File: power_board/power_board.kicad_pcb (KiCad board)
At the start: 2 copper layers, 171.8 x 117.7 mm, 86 parts, among them J1 PROG, J10 M4, J11 5V_1, J12 M5, J13 M6, J14 M7, J15 FAN, J16 Screw_Terminal_01x02, J17 MB_interface, J18 Conn_01x02_Female, J19 12V_1, J2 M1, J20 12V_2, J21 12V_3, J22 12V_4, J23 48V_1, J24 48V_2, J25 48V_3, J26 48V_4, J27 Screw_Terminal_01x02, J3 M2, J4 Conn_01x02_Female, J5 Conn_01x02_Female, J6 Conn_01x01_Male, J7 Conn_01x01_Male, J8 Screw_Terminal_01x02, J9 M3, Q1 Q_NPN_BEC, SW1 SW_Push, U1 ACS758xCB-050B-PFF, U10 MAX31855KASA, U2 ACS758xCB-050B-PFF, U3 MCP2515-EST, U4 MAX31855KASA, U5 ATA6560,1, U6 BTS50085-1TMA, U7 ATmega328P-AU, U8 BTS50085-1TMA, U9 LM2596S-5, Y1 20Mhz, Y2 16Mhz

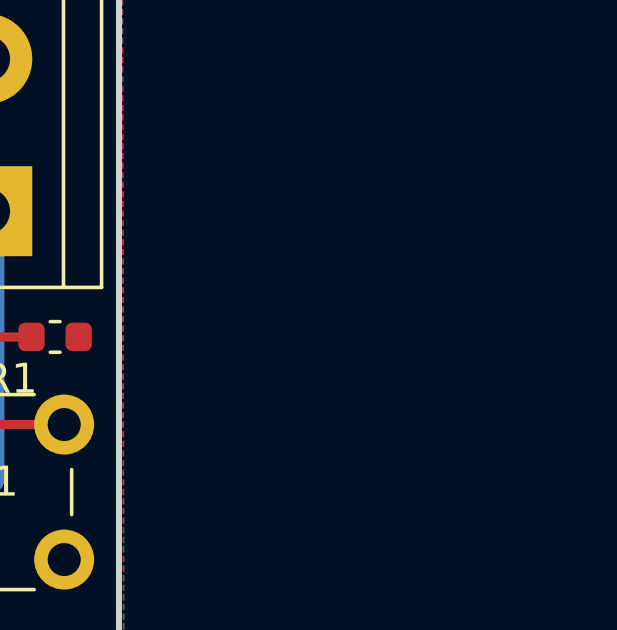
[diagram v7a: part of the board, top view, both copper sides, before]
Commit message: Adding 3.3v regulator hardware for TC amps
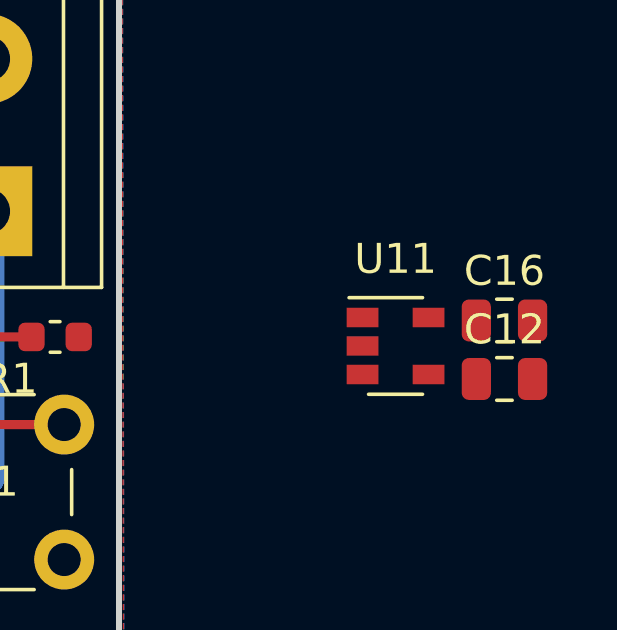
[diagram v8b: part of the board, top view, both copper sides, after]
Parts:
- added C12: 10uF, Capacitor_SMD:C_0805_2012Metric, F.Cu at (238.9, 72.1)
- added C16: 10uF, Capacitor_SMD:C_0805_2012Metric, F.Cu at (238.9, 70.2)
- added U11: TLV75533PDBV, Package_TO_SOT_SMD:SOT-23-5, F.Cu at (235.2, 71.0)
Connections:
- C10 pad 1: +5V -> V_MCU
- C5 pad 1: +5V -> V_MCU
- C6 pad 1: +5V -> +3V3
- C7 pad 1: +5V -> +3V3
- R10 pad 1: +5V -> +3V3
- R8 pad 1: +5V -> +3V3
- U10 pad 4: +5V -> +3V3
- U3 pad 20: +5V -> V_MCU
- U4 pad 4: +5V -> +3V3
- U5 pad 3: +5V -> V_MCU
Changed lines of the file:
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@@
     (tracks 867)
     (zones 0)
-    (modules 86)
-    (nets 68)
+    (modules 89)
+    (nets 70)
   )
   (page A4)
@@
   (net 66 V_MCU)
   (net 67 "Net-(R9-Pad1)")
+  (net 68 +3V3)
+  (net 69 "Net-(U11-Pad4)")
   (net_class Default "This is the default net class."
     (clearance 0.2)
@@
     (add_net +12V)
     (add_net +12VA)
+    (add_net +3V3)
     (add_net +48V)
     (add_net +5V)
@@
     (add_net "Net-(REG1-Pad5)")
     (add_net "Net-(REG2-Pad5)")
+    (add_net "Net-(U11-Pad4)")
     (add_net "Net-(U3-Pad3)")
     (add_net "Net-(U3-Pad6)")
@@
     (add_net V_MCU)
   )
+  (module Capacitor_SMD:C_0805_2012Metric (layer F.Cu)
+    (at 238.854001 72.140001)
+    (descr "Capacitor SMD 0805 (2012 Metric), square (rectangular) end terminal, IPC_7351 nominal, (Body size source: https://docs.google.com/spreadsheets/d/1BsfQQcO9C6DZCsRaXUlFlo91Tg2WpOkGARC1WS5S8t0/edit?usp=sharing), generated with kicad-footprint-generator")
+    (tags capacitor)
+    (attr smd)
+    (fp_text reference C12 (at 0 -1.65) (layer F.SilkS)
+      (effects (font (size 1 1) (thickness 0.15)))
+    )
+    (fp_text value 10uF (at 0 1.65) (layer F.Fab)
+      (effects (font (size 1 1) (thickness 0.15)))
+    )
+    (fp_text user %R (at 0 0) (layer F.Fab)
+      (effects (font (size 0.5 0.5) (thickness 0.08)))
+    )
+    (fp_line (start 1.68 0.95) (end -1.68 0.95) (layer F.CrtYd) (width 0.05))
+    (fp_line (start 1.68 -0.95) (end 1.68 0.95) (layer F.CrtYd) (width 0.05))
+    (fp_line (start -1.68 -0.95) (end 1.68 -0.95) (layer F.CrtYd) (width 0.05))
+    (fp_line (start -1.68 0.95) (end -1.68 -0.95) (layer F.CrtYd) (width 0.05))
+    (fp_line (start -0.258578 0.71) (end 0.258578 0.71) (layer F.SilkS) (width 0.12))
+    (fp_line (start -0.258578 -0.71) (end 0.258578 -0.71) (layer F.SilkS) (width 0.12))
+    (fp_line (start 1 0.6) (end -1 0.6) (layer F.Fab) (width 0.1))
+    (fp_line (start 1 -0.6) (end 1 0.6) (layer F.Fab) (width 0.1))
+    (fp_line (start -1 -0.6) (end 1 -0.6) (layer F.Fab) (width 0.1))
+    (fp_line (start -1 0.6) (end -1 -0.6) (layer F.Fab) (width 0.1))
+    (pad 2 smd roundrect (at 0.9375 0) (size 0.975 1.4) (layers F.Cu F.Paste F.Mask) (roundrect_rratio 0.25)
+      (net 5 GNDREF))
+    (pad 1 smd roundrect (at -0.9375 0) (size 0.975 1.4) (layers F.Cu F.Paste F.Mask) (roundrect_rratio 0.25)
+      (net 66 V_MCU))
+    (model ${KISYS3DMOD}/Capacitor_SMD.3dshapes/C_0805_2012Metric.wrl
+      (at (xyz 0 0 0))
+      (scale (xyz 1 1 1))
+      (rotate (xyz 0 0 0))
+    )
+  )
+  (module Capacitor_SMD:C_0805_2012Metric (layer F.Cu)
+    (at 238.854001 70.190001)
+    (descr "Capacitor SMD 0805 (2012 Metric), square (rectangular) end terminal, IPC_7351 nominal, (Body size source: https://docs.google.com/spreadsheets/d/1BsfQQcO9C6DZCsRaXUlFlo91Tg2WpOkGARC1WS5S8t0/edit?usp=sharing), generated with kicad-footprint-generator")
+    (tags capacitor)
+    (attr smd)
+    (fp_text reference C16 (at 0 -1.65) (layer F.SilkS)
+      (effects (font (size 1 1) (thickness 0.15)))
+    )
+    (fp_text value 10uF (at 0 1.65) (layer F.Fab)
+      (effects (font (size 1 1) (thickness 0.15)))
+    )
+    (fp_line (start -1 0.6) (end -1 -0.6) (layer F.Fab) (width 0.1))
+    (fp_line (start -1 -0.6) (end 1 -0.6) (layer F.Fab) (width 0.1))
+    (fp_line (start 1 -0.6) (end 1 0.6) (layer F.Fab) (width 0.1))
+    (fp_line (start 1 0.6) (end -1 0.6) (layer F.Fab) (width 0.1))
+    (fp_line (start -0.258578 -0.71) (end 0.258578 -0.71) (layer F.SilkS) (width 0.12))
+    (fp_line (start -0.258578 0.71) (end 0.258578 0.71) (layer F.SilkS) (width 0.12))
+    (fp_line (start -1.68 0.95) (end -1.68 -0.95) (layer F.CrtYd) (width 0.05))
+    (fp_line (start -1.68 -0.95) (end 1.68 -0.95) (layer F.CrtYd) (width 0.05))
+    (fp_line (start 1.68 -0.95) (end 1.68 0.95) (layer F.CrtYd) (width 0.05))
+    (fp_line (start 1.68 0.95) (end -1.68 0.95) (layer F.CrtYd) (width 0.05))
+    (fp_text user %R (at 0 0) (layer F.Fab)
+      (effects (font (size 0.5 0.5) (thickness 0.08)))
+    )
+    (pad 1 smd roundrect (at -0.9375 0) (size 0.975 1.4) (layers F.Cu F.Paste F.Mask) (roundrect_rratio 0.25)
+      (net 68 +3V3))
+    (pad 2 smd roundrect (at 0.9375 0) (size 0.975 1.4) (layers F.Cu F.Paste F.Mask) (roundrect_rratio 0.25)
+      (net 5 GNDREF))
+    (model ${KISYS3DMOD}/Capacitor_SMD.3dshapes/C_0805_2012Metric.wrl
+      (at (xyz 0 0 0))
+      (scale (xyz 1 1 1))
+      (rotate (xyz 0 0 0))
+    )
+  )
+  (module Package_TO_SOT_SMD:SOT-23-5 (layer F.Cu)
+    (at 235.224001 71.040001)
+    (descr "5-pin SOT23 package")
+    (tags SOT-23-5)
+    (attr smd)
+    (fp_text reference U11 (at 0 -2.9) (layer F.SilkS)
+      (effects (font (size 1 1) (thickness 0.15)))
+    )
+    (fp_text value TLV75533PDBV (at 0 2.9) (layer F.Fab)
+      (effects (font (size 1 1) (thickness 0.15)))
+    )
+    (fp_text user %R (at 0 0 90) (layer F.Fab)
+      (effects (font (size 0.5 0.5) (thickness 0.075)))
+    )
+    (fp_line (start -0.9 1.61) (end 0.9 1.61) (layer F.SilkS) (width 0.12))
+    (fp_line (start 0.9 -1.61) (end -1.55 -1.61) (layer F.SilkS) (width 0.12))
+    (fp_line (start -1.9 -1.8) (end 1.9 -1.8) (layer F.CrtYd) (width 0.05))
+    (fp_line (start 1.9 -1.8) (end 1.9 1.8) (layer F.CrtYd) (width 0.05))
+    (fp_line (start 1.9 1.8) (end -1.9 1.8) (layer F.CrtYd) (width 0.05))
+    (fp_line (start -1.9 1.8) (end -1.9 -1.8) (layer F.CrtYd) (width 0.05))
+    (fp_line (start -0.9 -0.9) (end -0.25 -1.55) (layer F.Fab) (width 0.1))
+    (fp_line (start 0.9 -1.55) (end -0.25 -1.55) (layer F.Fab) (width 0.1))
+    (fp_line (start -0.9 -0.9) (end -0.9 1.55) (layer F.Fab) (width 0.1))
+    (fp_line (start 0.9 1.55) (end -0.9 1.55) (layer F.Fab) (width 0.1))
+    (fp_line (start 0.9 -1.55) (end 0.9 1.55) (layer F.Fab) (width 0.1))
+    (pad 1 smd rect (at -1.1 -0.95) (size 1.06 0.65) (layers F.Cu F.Paste F.Mask)
+      (net 66 V_MCU))
+    (pad 2 smd rect (at -1.1 0) (size 1.06 0.65) (layers F.Cu F.Paste F.Mask)
+      (net 5 GNDREF))
+    (pad 3 smd rect (at -1.1 0.95) (size 1.06 0.65) (layers F.Cu F.Paste F.Mask)
+      (net 66 V_MCU))
+    (pad 4 smd rect (at 1.1 0.95) (size 1.06 0.65) (layers F.Cu F.Paste F.Mask)
+      (net 69 "Net-(U11-Pad4)"))
+    (pad 5 smd rect (at 1.1 -0.95) (size 1.06 0.65) (layers F.Cu F.Paste F.Mask)
+      (net 68 +3V3))
+    (model ${KISYS3DMOD}/Package_TO_SOT_SMD.3dshapes/SOT-23-5.wrl
+      (at (xyz 0 0 0))
+      (scale (xyz 1 1 1))
+      (rotate (xyz 0 0 0))
+    )
+  )
   (module Diode_SMD:D_SMC (layer F.Cu)
     (at 179.1752 56.134 180)
@@
     )
     (pad 1 smd roundrect (at -0.7875 0 90) (size 0.875 0.95) (layers F.Cu F.Paste F.Mask) (roundrect_rratio 0.25)
-      (net 3 +5V))
+      (net 68 +3V3))
     (pad 2 smd roundrect (at 0.7875 0 90) (size 0.875 0.95) (layers F.Cu F.Paste F.Mask) (roundrect_rratio 0.25)
       (net 5 GNDREF))
@@
       (net 64 "Net-(J27-Pad2)"))
     (pad 4 smd rect (at -2.7 1.905 180) (size 1.55 0.6) (layers F.Cu F.Paste F.Mask)
-      (net 3 +5V))
+      (net 68 +3V3))
     (pad 5 smd rect (at 2.7 1.905 180) (size 1.55 0.6) (layers F.Cu F.Paste F.Mask)
       (net 21 SCK))
@@
     )
     (pad 1 smd roundrect (at -0.7875 0 180) (size 0.875 0.95) (layers F.Cu F.Paste F.Mask) (roundrect_rratio 0.25)
-      (net 3 +5V))
+      (net 68 +3V3))
     (pad 2 smd roundrect (at 0.7875 0 180) (size 0.875 0.95) (layers F.Cu F.Paste F.Mask) (roundrect_rratio 0.25)
       (net 61 TC2_CS))
@@
       (net 5 GNDREF))
     (pad 1 smd roundrect (at -0.7875 0 270) (size 0.875 0.95) (layers F.Cu F.Paste F.Mask) (roundrect_rratio 0.25)
-      (net 3 +5V))
+      (net 66 V_MCU))
     (model ${KISYS3DMOD}/Capacitor_SMD.3dshapes/C_0603_1608Metric.wrl
       (at (xyz 0 0 0))
@@
       (net 5 GNDREF))
     (pad 1 smd roundrect (at -0.7875 0 90) (size 0.875 0.95) (layers F.Cu F.Paste F.Mask) (roundrect_rratio 0.25)
-      (net 3 +5V))
+      (net 68 +3V3))
     (model ${KISYS3DMOD}/Capacitor_SMD.3dshapes/C_0603_1608Metric.wrl
       (at (xyz 0 0 0))
@@
       (net 5 GNDREF))
     (pad 1 smd roundrect (at -0.7875 0 90) (size 0.875 0.95) (layers F.Cu F.Paste F.Mask) (roundrect_rratio 0.25)
-      (net 3 +5V))
+      (net 66 V_MCU))
     (model ${KISYS3DMOD}/Capacitor_SMD.3dshapes/C_0603_1608Metric.wrl
       (at (xyz 0 0 0))
@@
       (net 15 CAN_RX))
     (pad 3 smd rect (at -2.7 0.635) (size 1.55 0.6) (layers F.Cu F.Paste F.Mask)
-      (net 3 +5V))
+      (net 66 V_MCU))
     (pad 2 smd rect (at -2.7 -0.635) (size 1.55 0.6) (layers F.Cu F.Paste F.Mask)
       (net 5 GNDREF))
@@
       (net 35 "Net-(J8-Pad2)"))
     (pad 4 smd rect (at -2.7 1.905 180) (size 1.55 0.6) (layers F.Cu F.Paste F.Mask)
-      (net 3 +5V))
+      (net 68 +3V3))
     (pad 5 smd rect (at 2.7 1.905 180) (size 1.55 0.6) (layers F.Cu F.Paste F.Mask)
       (net 21 SCK))
@@
       (net 13 RESET))
     (pad 20 smd rect (at 2.95 -2.925 270) (size 1.45 0.45) (layers F.Cu F.Paste F.Mask)
-      (net 3 +5V))
+      (net 66 V_MCU))
     (model ${KISYS3DMOD}/Package_SO.3dshapes/TSSOP-20_4.4x6.5mm_P0.65mm.wrl
       (at (xyz 0 0 0))
@@
     )
     (pad 1 smd roundrect (at -0.7875 0 180) (size 0.875 0.95) (layers F.Cu F.Paste F.Mask) (roundrect_rratio 0.25)
-      (net 3 +5V))
+      (net 68 +3V3))
     (pad 2 smd roundrect (at 0.7875 0 180) (size 0.875 0.95) (layers F.Cu F.Paste F.Mask) (roundrect_rratio 0.25)
       (net 62 TC1_CS))
